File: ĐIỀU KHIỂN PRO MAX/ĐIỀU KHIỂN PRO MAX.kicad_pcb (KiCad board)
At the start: 2 copper layers, 10 parts, among them U1 NRF24L01_Breakout, U2 ESP32-DevKitC

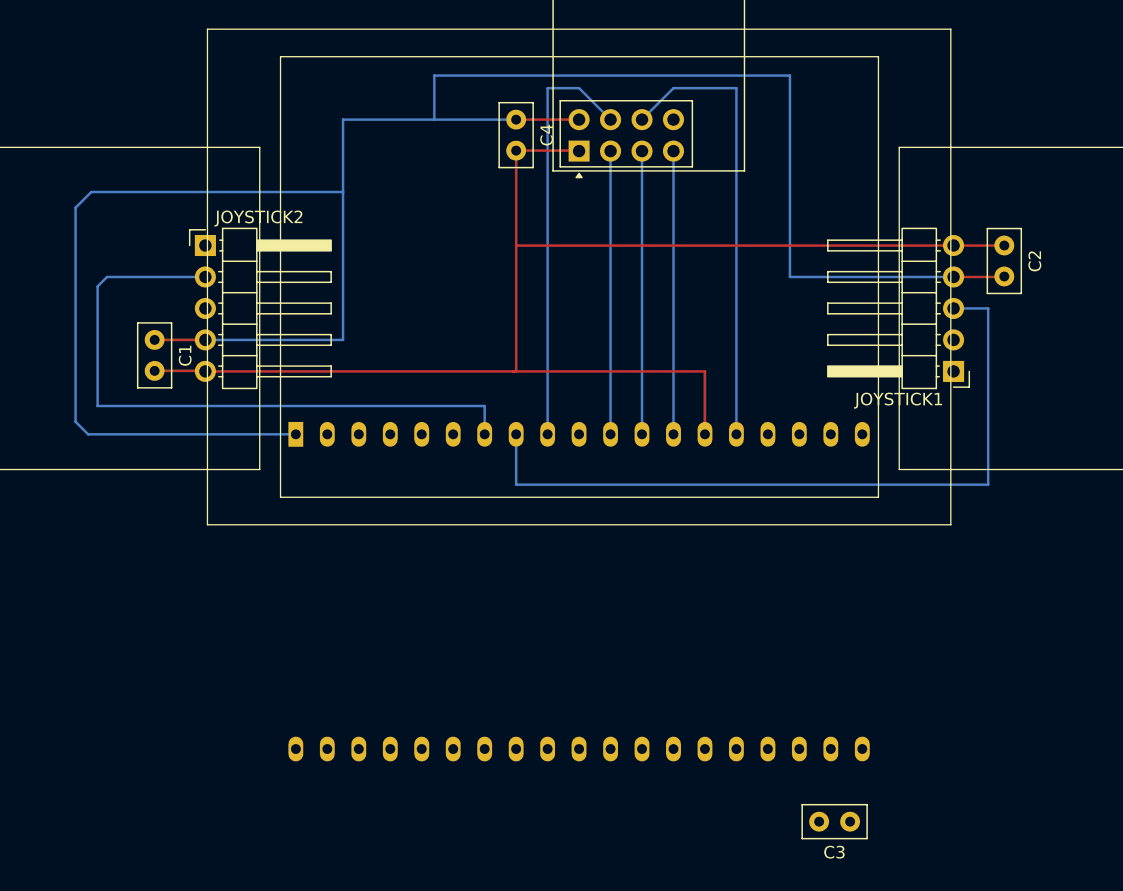
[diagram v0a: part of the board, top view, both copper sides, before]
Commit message: Finished Controller PCB optimization and soldered 2 controllers
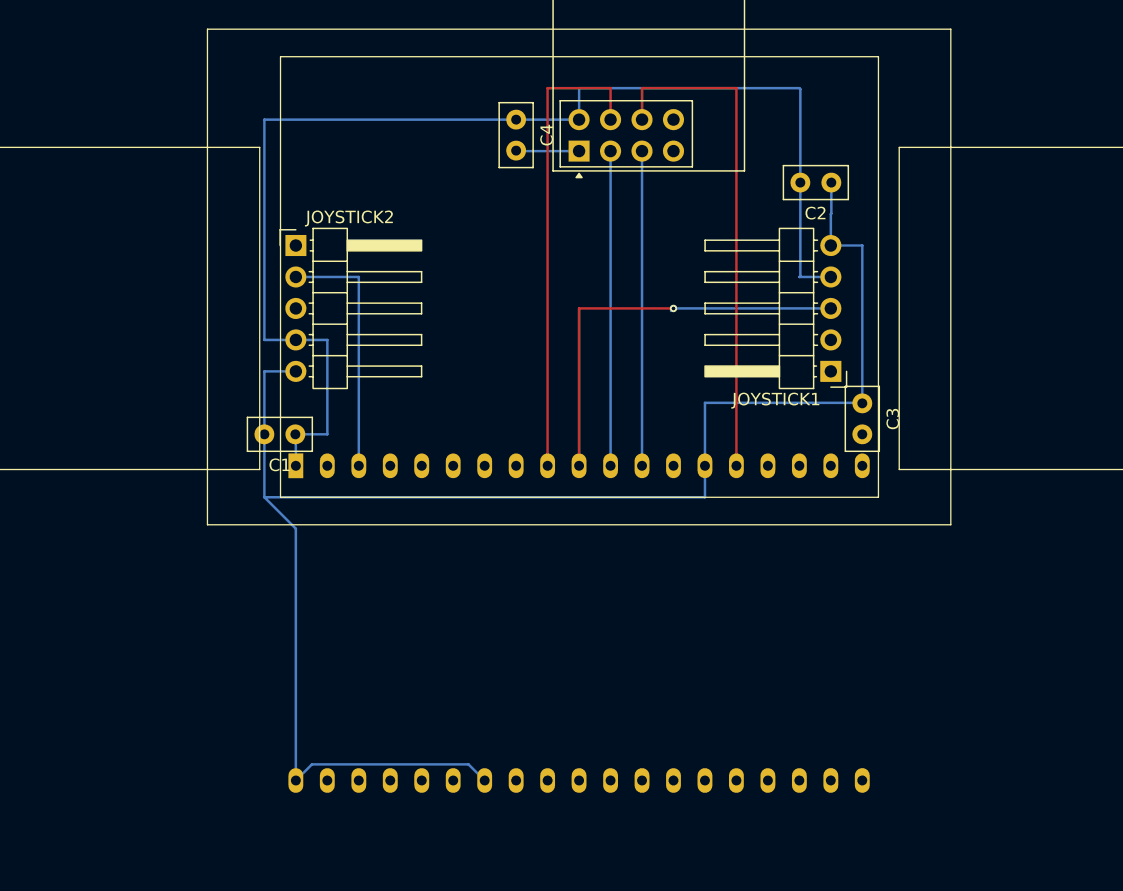
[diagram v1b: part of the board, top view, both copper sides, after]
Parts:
- moved C3 33.8 mm to (152.4, 106.7), turned to -90 degrees
- moved C2 14.9 mm to (149.9, 88.9), turned to 180 degrees
- moved C1 13.7 mm to (106.6, 109.2), turned to 180 degrees
- moved JOYSTICK1 9.91 mm to (149.9, 104.1)
- moved JOYSTICK2 7.30 mm to (106.7, 94.0)
- moved U2 2.54 mm to (106.7, 111.8)
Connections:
- JOYSTICK1 pad 1: (no net) -> unconnected-(JOYSTICK1-SW-Pad1)
- JOYSTICK1 pad 2: (no net) -> unconnected-(JOYSTICK1-VRY-Pad2)
- JOYSTICK2 pad 1: (no net) -> unconnected-(JOYSTICK2-SW-Pad1)
- JOYSTICK2 pad 3: (no net) -> unconnected-(JOYSTICK2-VRX-Pad3)
- U1 pad 7: MISO -> unconnected-(U1-MISO-Pad7)
- U2 pad 10: unconnected-(U2-DAC_2/ADC2_CH9/GPIO26-Pad10) -> VRX1
- U2 pad 13: MISO -> unconnected-(U2-MTDI/GPIO12/ADC2_CH5-Pad13)
- U2 pad 3: unconnected-(U2-SENSOR_VP/GPIO36/ADC1_CH0-Pad3) -> VRY2
- U2 pad 7: VRY2 -> unconnected-(U2-32K_XP/GPIO32/ADC1_CH4-Pad7)
- U2 pad 8: VRX1 -> unconnected-(U2-32K_XN/GPIO33/ADC1_CH5-Pad8)
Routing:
- net +3V3: track 175.5 -> 99.2 mm
- net VRY2: track 52.2 -> 20.3 mm
- net VRX1: track 59.2 -> 33.3 mm, vias 0 -> 1
- net MISO: track 22.9 -> 0.00 mm
- net GND: track 112.4 -> 134.3 mm
- net CSN: track 34.1 -> 38.1 mm
- net MOSI: track 36.6 -> 40.6 mm
- net SCK: track 22.9 -> 25.4 mm
- net CE: track 22.9 -> 25.4 mm

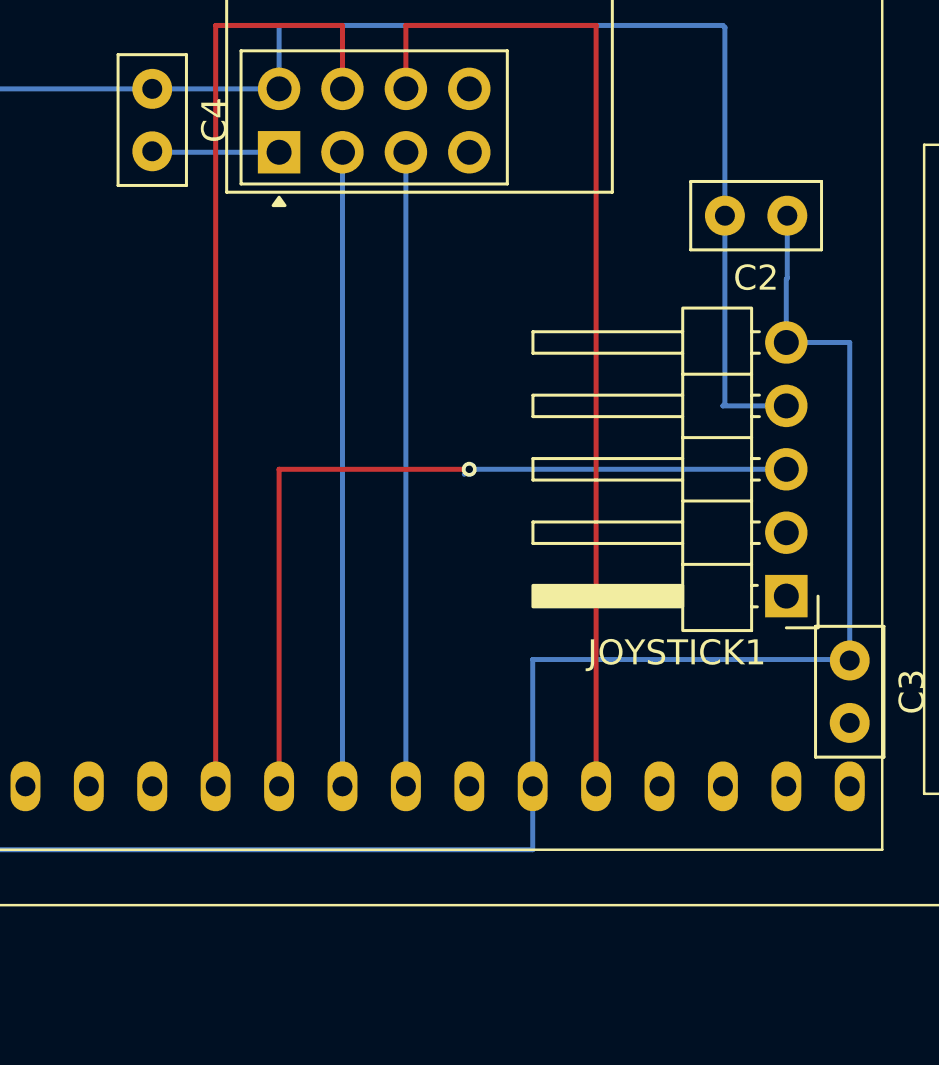
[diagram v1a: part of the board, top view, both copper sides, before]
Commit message: Successfully initialized NRF on Controllers. MISO MOSI required for PCB.
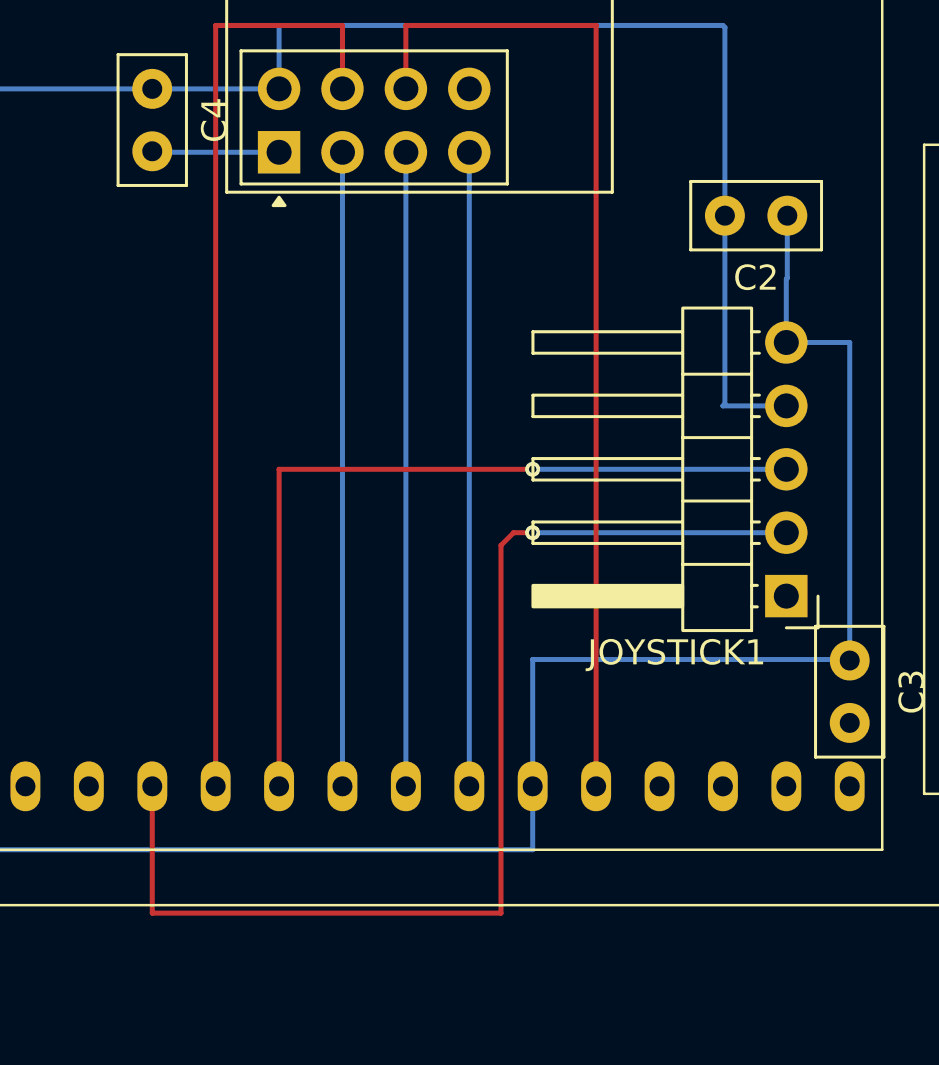
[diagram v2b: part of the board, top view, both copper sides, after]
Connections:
- JOYSTICK1 pad 2: unconnected-(JOYSTICK1-VRY-Pad2) -> VRY1
- U1 pad 7: unconnected-(U1-MISO-Pad7) -> MISO
- U2 pad 13: unconnected-(U2-MTDI/GPIO12/ADC2_CH5-Pad13) -> MISO
- U2 pad 8: unconnected-(U2-32K_XN/GPIO33/ADC1_CH5-Pad8) -> VRY1
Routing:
- net VRY1: track 0.00 -> 45.4 mm, vias 0 -> 1
- net MISO: track 0.00 -> 25.4 mm
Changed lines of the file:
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@@
 			(layers "*.Cu" "*.Mask")
 			(remove_unused_layers no)
-			(net "unconnected-(U1-MISO-Pad7)")
+			(net "MISO")
 			(pinfunction "MISO_7")
-			(pintype "output+no_connect")
+			(pintype "output")
 		)
 		(pad "8" thru_hole circle
@@
 			(layers "*.Cu" "*.Mask")
 			(remove_unused_layers no)
-			(net "unconnected-(JOYSTICK1-VRY-Pad2)")
+			(net "VRY1")
 			(pinfunction "VRY_2")
-			(pintype "output+no_connect")
+			(pintype "output")
 		)
 		(pad "3" thru_hole circle
@@
 			(layers "*.Cu" "*.Mask")
 			(remove_unused_layers no)
-			(net "unconnected-(U2-32K_XN{slash}GPIO33{slash}ADC1_CH5-Pad8)")
+			(net "VRY1")
 			(pinfunction "32K_XN/GPIO33/ADC1_CH5_8")
 			(pintype "bidirectional")
@@
 			(layers "*.Cu" "*.Mask")
 			(remove_unused_layers no)
-			(net "unconnected-(U2-MTDI{slash}GPIO12{slash}ADC2_CH5-Pad13)")
+			(net "MISO")
 			(pinfunction "MTDI/GPIO12/ADC2_CH5_13")
-			(pintype "bidirectional+no_connect")
+			(pintype "bidirectional")
 		)
 		(pad "14" thru_hole oval
@@
 	)
 	(segment
+		(start 139.7 99.06)
+		(end 129.54 99.06)
+		(width 0.2)
+		(layer "F.Cu")
+		(net "VRX1")
+	)
+	(segment
 		(start 129.54 99.06)
 		(end 129.54 111.76)
@@
 		(net "VRX1")
 	)
-	(segment
-		(start 137.16 99.06)
-		(end 129.54 99.06)
-		(width 0.2)
-		(layer "F.Cu")
-		(net "VRX1")
-	)
 	(via
-		(at 137.16 99.06)
+		(at 139.7 99.06)
 		(size 0.6)
 		(drill 0.3)
@@
 	(segment
 		(start 149.86 99.06)
-		(end 137.16 99.06)
+		(end 139.7 99.06)
 		(width 0.2)
 		(layer "B.Cu")
@@
 	)
 	(segment
-		(start 137.16 99.06)
-		(end 136.96 99.26)
-		(width 0.2)
-		(layer "B.Cu")
-		(net "VRX1")
+		(start 137.16 86.36)
+		(end 137.16 111.76)
+		(width 0.2)
+		(layer "B.Cu")
+		(net "MISO")
+	)
+	(segment
+		(start 124.46 116.84)
+		(end 124.46 111.76)
+		(width 0.2)
+		(layer "F.Cu")
+		(net "VRY1")
+	)
+	(segment
+		(start 138.43 116.84)
+		(end 124.46 116.84)
+		(width 0.2)
+		(layer "F.Cu")
+		(net "VRY1")
+	)
+	(segment
+		(start 139.7 101.6)
+		(end 138.938 101.6)
+		(width 0.2)
+		(layer "F.Cu")
+		(net "VRY1")
+	)
+	(segment
+		(start 138.43 102.108)
+		(end 138.43 116.84)
+		(width 0.2)
+		(layer "F.Cu")
+		(net "VRY1")
+	)
+	(segment
+		(start 138.938 101.6)
+		(end 138.43 102.108)
+		(width 0.2)
+		(layer "F.Cu")
+		(net "VRY1")
+	)
+	(via
+		(at 139.7 101.6)
+		(size 0.6)
+		(drill 0.3)
+		(layers "F.Cu" "B.Cu")
+		(net "VRY1")
+	)
+	(segment
+		(start 149.86 101.6)
+		(end 139.7 101.6)
+		(width 0.2)
+		(layer "B.Cu")
+		(net "VRY1")
 	)
 	(embedded_fonts no)

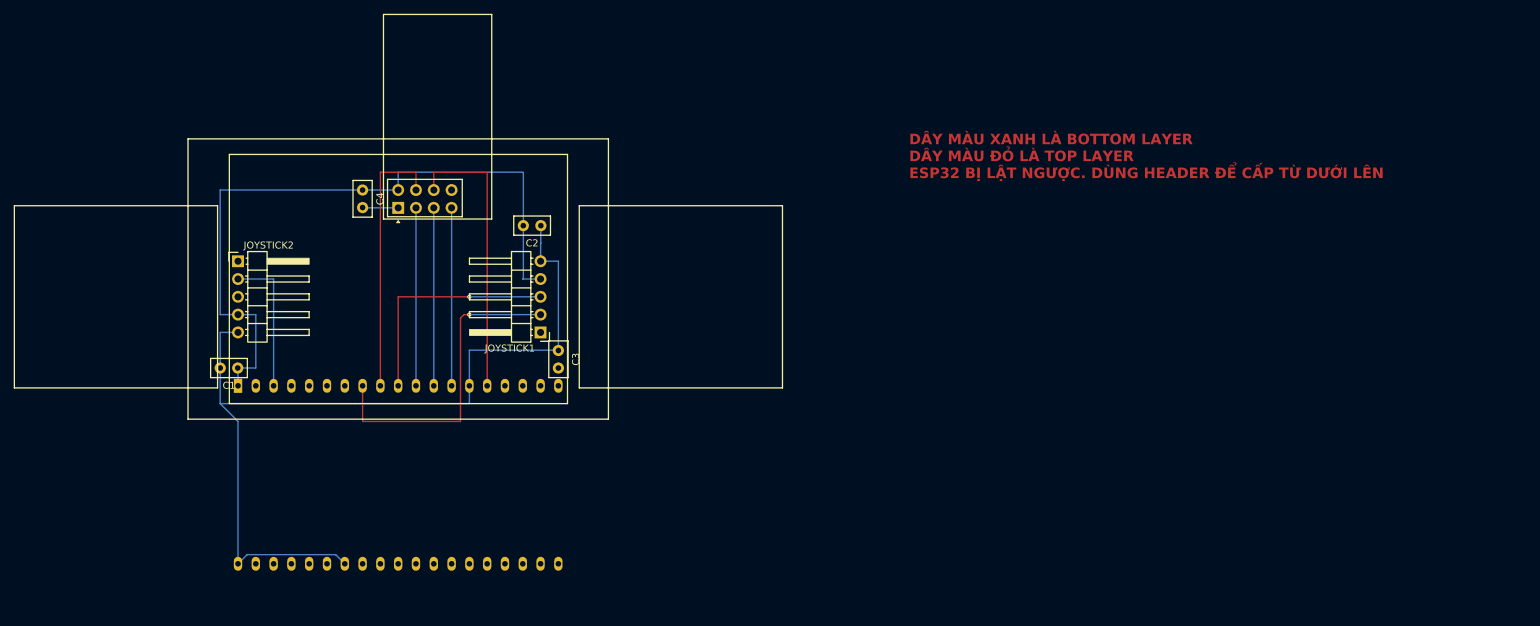
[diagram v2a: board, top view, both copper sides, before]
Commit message: Fixed DRC and added LDO, wires, fixed edge cuts
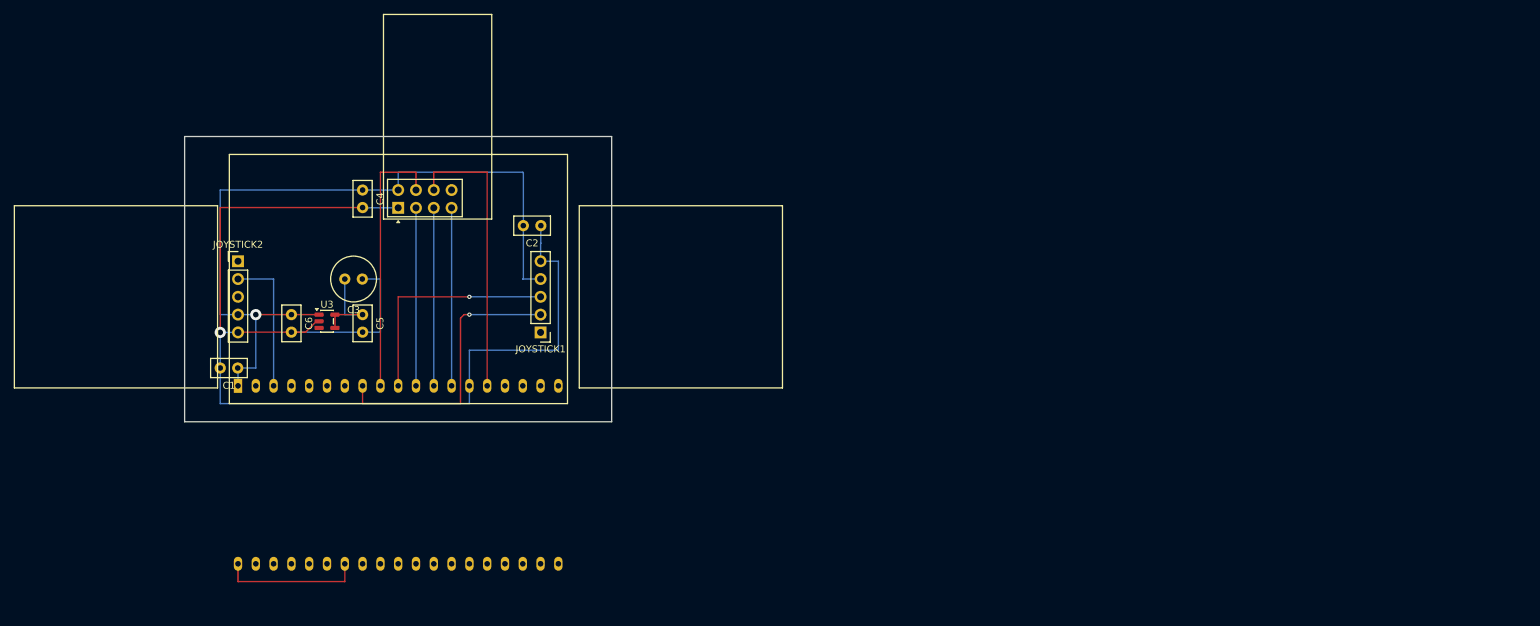
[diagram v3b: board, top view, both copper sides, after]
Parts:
- added C5: 100nF, Capacitor_THT:C_Disc_D5.0mm_W2.5mm_P2.50mm, F.Cu at (124.5, 101.6)
- added C6: 100nF, Capacitor_THT:C_Disc_D5.0mm_W2.5mm_P2.50mm, F.Cu at (114.3, 101.6)
- added U3: RT9013-33GB, Package_TO_SOT_SMD:TSOT-23-5, F.Cu at (119.4, 102.5)
- C3: footprint Capacitor_THT:C_Disc_D5.0mm_W2.5mm_P2.50mm -> Capacitor_THT:C_Radial_D6.3mm_H11.0mm_P2.50mm
- JOYSTICK1, JOYSTICK2: footprint Connector_PinHeader_2.54mm:PinHeader_1x05_P2.54mm_Horizontal -> Connector_PinHeader_2.54mm:PinHeader_1x05_P2.54mm_Vertical
- moved C3 29.8 mm to (124.4, 96.5), turned to 180 degrees
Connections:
- U2 pad 19: +5V -> unconnected-(U2-5V-Pad19)
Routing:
- net GND: track 134.3 -> 187.6 mm, vias 0 -> 1
- net +5V: track 0.00 -> 13.5 mm
- net +3V3: track 99.2 -> 108.2 mm, vias 0 -> 1
- net VRY1: track 45.4 -> 40.3 mm
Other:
- board outline added: 60.9 x 40.7 mm
